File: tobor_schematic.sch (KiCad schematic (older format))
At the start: 25 parts, among them SW1 Bin detect right, SW2 Bin detect left, U1 LM7805_TO220, U10 TCRT5000, U2 LM7833_TO220, U3 LM7805_TO220, U4 TCRT5000, U5 TCRT5000

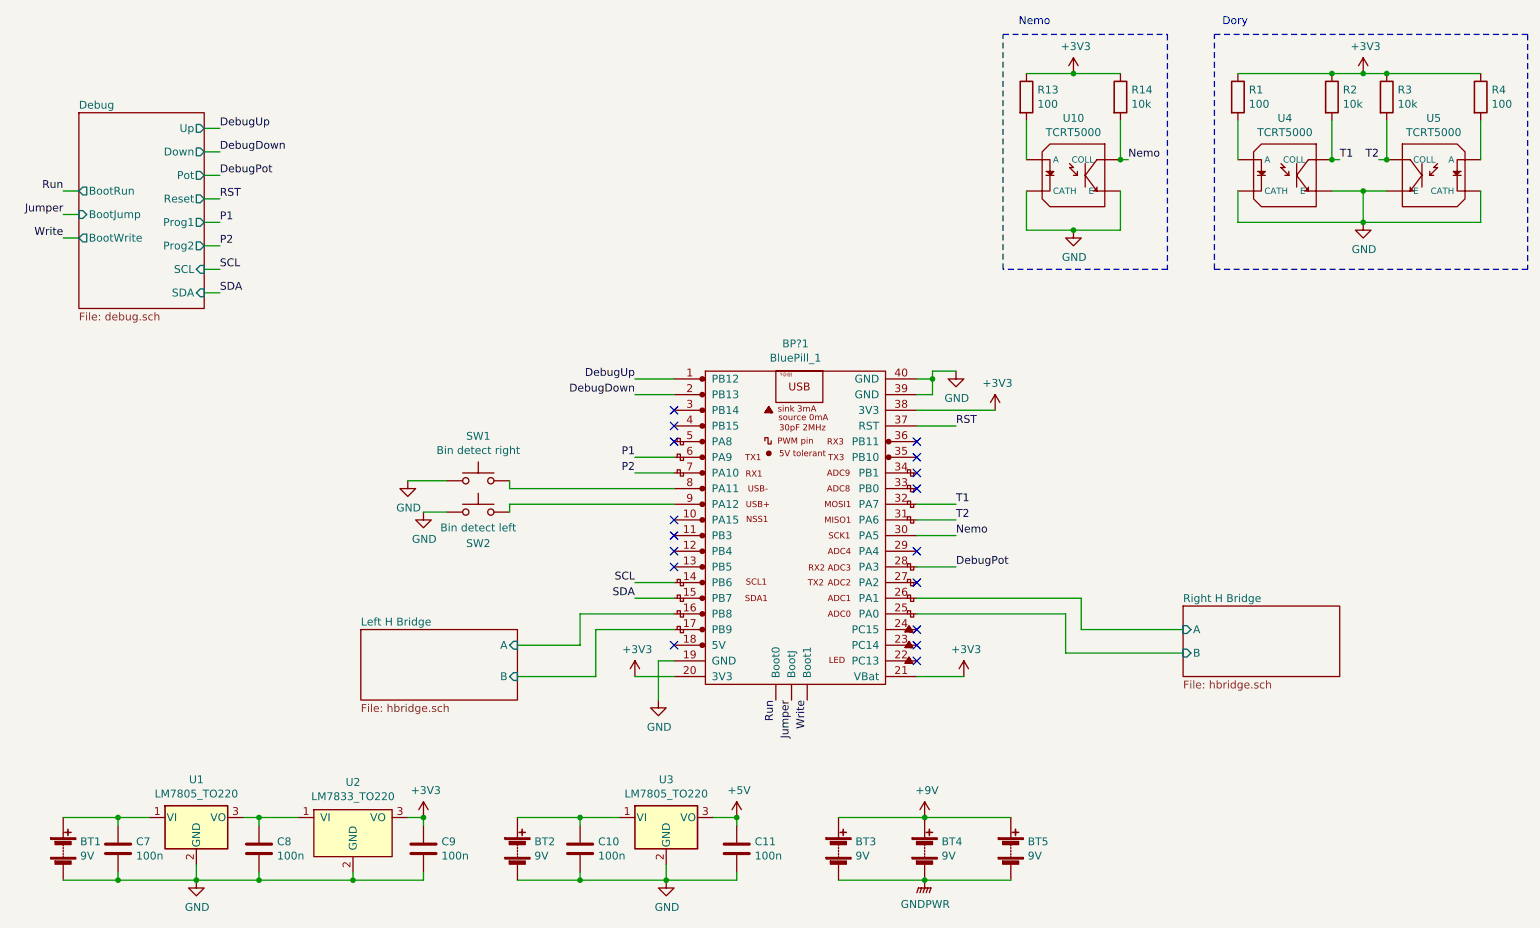
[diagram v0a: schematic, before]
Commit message: Add servos and can brush motor
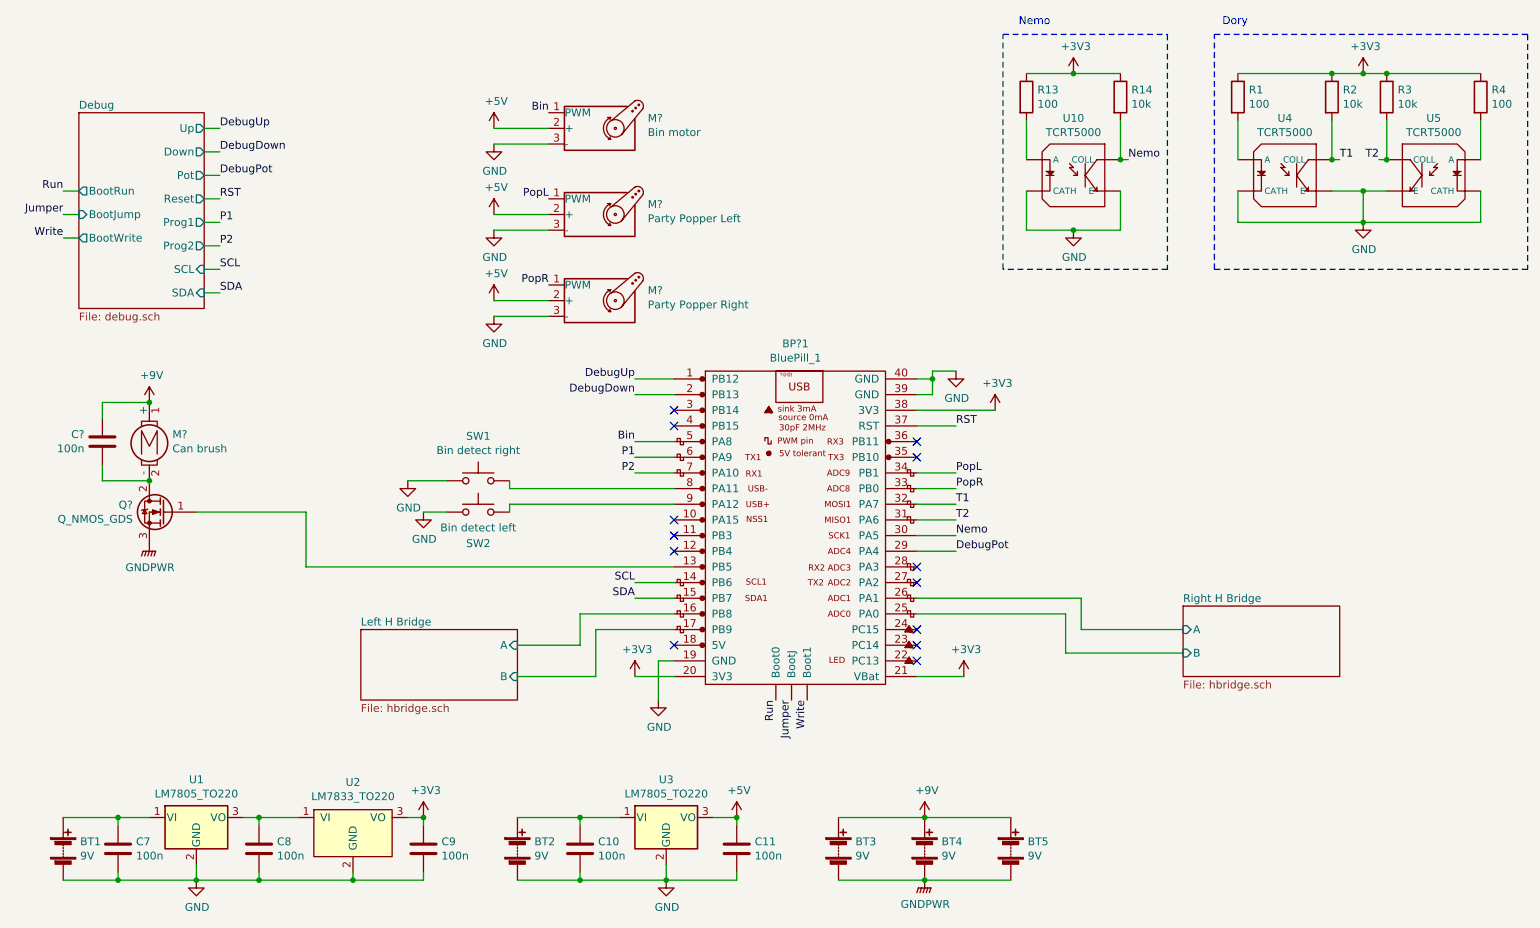
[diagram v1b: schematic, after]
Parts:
- added C?: 100n, symbol Device:C
- added M?: Bin motor, symbol Motor:Motor_Servo
- added M?: Party Popper Left, symbol Motor:Motor_Servo
- added M?: Party Popper Right, symbol Motor:Motor_Servo
- added M?: Can brush, symbol Motor:Motor_DC_ALT
- added Q?: Q_NMOS_GDS, symbol Device:Q_NMOS_GDS
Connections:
- net +5V: now also M?.2 (+), M?.2 (+), M?.2 (+)
- net +9V: now also C?.2, M?.1 (+)
- net DebugPot: now also BP?1.29 (PA4); no longer BP?1.28 (PA3)
- net GND: now also M?.3 (-), M?.3 (-), M?.3 (-)
- net GNDPWR: now also Q?.3 (S)
- net at BP?1.13 (PB5): now also Q?.1 (G)
- net PopR: now reaches BP?1.33 (PB0)
- net PopR: now also M?.1 (PWM)
- net PopL: now reaches BP?1.34 (PB1)
- net PopL: now also M?.1 (PWM)
- net Bin: now reaches BP?1.5 (PA8)
- net Bin: now also M?.1 (PWM)
- new net: C?.1, M?.2 (-), Q?.2 (D)
- no-connect marks 17 -> 13
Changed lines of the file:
@@
 NoConn ~ 5200 3250
 NoConn ~ 5200 3350
-NoConn ~ 5200 4250
 NoConn ~ 5200 4750
 NoConn ~ 6750 4850
@@
 Wire Wire Line
 	7000 4050 6750 4050
-Text Label 7000 4250 0    50   ~ 0
+Text Label 7000 4150 0    50   ~ 0
 DebugPot
-Wire Wire Line
-	7000 4250 6750 4250
 $Comp
 L STM32:BluePill_1 BP?1
@@
 NoConn ~ 5200 3950
 NoConn ~ 5200 4050
-NoConn ~ 5200 3450
-NoConn ~ 6750 3650
-NoConn ~ 6750 3750
-NoConn ~ 6750 4150
 Wire Wire Line
 	2200 1450 2300 1450
@@
 Wire Wire Line
 	6750 3250 7250 3250
+Wire Wire Line
+	7000 4150 6750 4150
+NoConn ~ 6750 4250
+$Comp
+L Motor:Motor_Servo M?
+U 1 1 5F00F8D5
+P 4700 1450
+F 0 "M?" H 5032 1515 50  0000 L CNN
+F 1 "Bin motor" H 5032 1424 50  0000 L CNN
+F 2 "" H 4700 1260 50  0001 C CNN
+F 3 "http://forums.parallax.com/uploads/attachments/46831/74481.png" H 4700 1260 50  0001 C CNN
+	1    4700 1450
+	1    0    0    -1
+$EndComp
+$Comp
+L Motor:Motor_Servo M?
+U 1 1 5F0107C0
+P 4700 2000
+F 0 "M?" H 5032 2065 50  0000 L CNN
+F 1 "Party Popper Left" H 5032 1974 50  0000 L CNN
+F 2 "" H 4700 1810 50  0001 C CNN
+F 3 "http://forums.parallax.com/uploads/attachments/46831/74481.png" H 4700 1810 50  0001 C CNN
+	1    4700 2000
+	1    0    0    -1
+$EndComp
+$Comp
+L Motor:Motor_Servo M?
+U 1 1 5F011350
+P 4700 2550
+F 0 "M?" H 5032 2615 50  0000 L CNN
+F 1 "Party Popper Right" H 5032 2524 50  0000 L CNN
+F 2 "" H 4700 2360 50  0001 C CNN
+F 3 "http://forums.parallax.com/uploads/attachments/46831/74481.png" H 4700 2360 50  0001 C CNN
+	1    4700 2550
+	1    0    0    -1
+$EndComp
+$Comp
+L power:+5V #PWR?
+U 1 1 5F0126EA
+P 4050 1450
+F 0 "#PWR?" H 4050 1300 50  0001 C CNN
+F 1 "+5V" H 4065 1623 50  0000 C CNN
+F 2 "" H 4050 1450 50  0001 C CNN
+F 3 "" H 4050 1450 50  0001 C CNN
+	1    4050 1450
+	1    0    0    -1
+$EndComp
+$Comp
+L power:+5V #PWR?
+U 1 1 5F012A59
+P 4050 2550
+F 0 "#PWR?" H 4050 2400 50  0001 C CNN
+F 1 "+5V" H 4065 2723 50  0000 C CNN
+F 2 "" H 4050 2550 50  0001 C CNN
+F 3 "" H 4050 2550 50  0001 C CNN
+	1    4050 2550
+	1    0    0    -1
+$EndComp
+$Comp
+L power:GND #PWR?
+U 1 1 5F01C8B6
+P 4050 1550
+F 0 "#PWR?" H 4050 1300 50  0001 C CNN
+F 1 "GND" H 4055 1377 50  0000 C CNN
+F 2 "" H 4050 1550 50  0001 C CNN
+F 3 "" H 4050 1550 50  0001 C CNN
+	1    4050 1550
+	1    0    0    -1
+$EndComp
+$Comp
+L power:GND #PWR?
+U 1 1 5F01CD54
+P 4050 2100
+F 0 "#PWR?" H 4050 1850 50  0001 C CNN
+F 1 "GND" H 4055 1927 50  0000 C CNN
+F 2 "" H 4050 2100 50  0001 C CNN
+F 3 "" H 4050 2100 50  0001 C CNN
+	1    4050 2100
+	1    0    0    -1
+$EndComp
+$Comp
+L power:+5V #PWR?
+U 1 1 5F0128A7
+P 4050 2000
+F 0 "#PWR?" H 4050 1850 50  0001 C CNN
+F 1 "+5V" H 4065 2173 50  0000 C CNN
+F 2 "" H 4050 2000 50  0001 C CNN
+F 3 "" H 4050 2000 50  0001 C CNN
+	1    4050 2000
+	1    0    0    -1
+$EndComp
+$Comp
+L power:GND #PWR?
+U 1 1 5F02E2B0
+P 4050 2650
+F 0 "#PWR?" H 4050 2400 50  0001 C CNN
+F 1 "GND" H 4055 2477 50  0000 C CNN
+F 2 "" H 4050 2650 50  0001 C CNN
+F 3 "" H 4050 2650 50  0001 C CNN
+	1    4050 2650
+	1    0    0    -1
+$EndComp
+Wire Wire Line
+	4050 2550 4400 2550
+Wire Wire Line
+	4400 2650 4050 2650
+Wire Wire Line
+	4050 2100 4400 2100
+Wire Wire Line
+	4400 2000 4050 2000
+Wire Wire Line
+	4050 1550 4400 1550
+Wire Wire Line
+	4400 1450 4050 1450
+Text Label 4400 1350 2    50   ~ 0
+Bin
+Text Label 4400 1900 2    50   ~ 0
+PopL
+Text Label 4400 2450 2    50   ~ 0
+PopR
+Text Label 4950 3450 2    50   ~ 0
+Bin
+Wire Wire Line
+	4950 3450 5200 3450
+Text Label 7000 3650 0    50   ~ 0
+PopL
+Text Label 7000 3750 0    50   ~ 0
+PopR
+Wire Wire Line
+	7000 3750 6750 3750
+Wire Wire Line
+	6750 3650 7000 3650
+$Comp
+L power:GNDPWR #PWR?
+U 1 1 5F0D4619
+P 1850 4100
+F 0 "#PWR?" H 1850 3900 50  0001 C CNN
+F 1 "GNDPWR" H 1854 3946 50  0000 C CNN
+F 2 "" H 1850 4050 50  0001 C CNN
+F 3 "" H 1850 4050 50  0001 C CNN
+	1    1850 4100
+	1    0    0    -1
+$EndComp
+$Comp
+L Device:Q_NMOS_GDS Q?
+U 1 1 5F0D2B87
+P 1950 3900
+F 0 "Q?" H 2156 3946 50  0000 L CNN
+F 1 "Q_NMOS_GDS" H 2156 3855 50  0000 L CNN
+F 2 "" H 2150 4000 50  0001 C CNN
+F 3 "~" H 1950 3900 50  0001 C CNN
+	1    1950 3900
+	-1   0    0    -1
+$EndComp
+Wire Wire Line
+	2150 3900 2850 3900
+Wire Wire Line
+	2850 3900 2850 4250
+Wire Wire Line
+	2850 4250 5200 4250
+$Comp
+L Motor:Motor_DC_ALT M?
+U 1 1 5F0ED853
+P 1850 3400
+F 0 "M?" H 1997 3396 50  0000 L CNN
+F 1 "Can brush" H 1997 3305 50  0000 L CNN
+F 2 "" H 1850 3310 50  0001 C CNN
+F 3 "~" H 1850 3310 50  0001 C CNN
+	1    1850 3400
+	1    0    0    -1
+$EndComp
+$Comp
+L Device:C C?
+U 1 1 5F0EEAE3
+P 1550 3450
+F 0 "C?" H 1435 3404 50  0000 R CNN
+F 1 "100n" H 1435 3495 50  0000 R CNN
+F 2 "" H 1588 3300 50  0001 C CNN
+F 3 "~" H 1550 3450 50  0001 C CNN
+	1    1550 3450
+	1    0    0    1
+$EndComp
+Wire Wire Line
+	1550 3600 1550 3700
+Wire Wire Line
+	1550 3700 1850 3700
+Connection ~ 1850 3700
+Wire Wire Line
+	1550 3300 1550 3200
+Wire Wire Line
+	1550 3200 1850 3200
+$Comp
+L power:+9V #PWR?
+U 1 1 5F0FAB23
+P 1850 3200
+F 0 "#PWR?" H 1850 3050 50  0001 C CNN
+F 1 "+9V" H 1865 3373 50  0000 C CNN
+F 2 "" H 1850 3200 50  0001 C CNN
+F 3 "" H 1850 3200 50  0001 C CNN
+	1    1850 3200
+	1    0    0    -1
+$EndComp
+Connection ~ 1850 3200
 $EndSCHEMATC

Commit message: Misc minor fixes
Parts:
- gave numbers to parts that had none: 6
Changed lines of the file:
@@
 NoConn ~ 6750 4250
 $Comp
-L Motor:Motor_Servo M?
+L Motor:Motor_Servo M4
 U 1 1 5F00F8D5
 P 4700 1450
-F 0 "M?" H 5032 1515 50  0000 L CNN
+F 0 "M4" H 5032 1515 50  0000 L CNN
 F 1 "Bin motor" H 5032 1424 50  0000 L CNN
 F 2 "" H 4700 1260 50  0001 C CNN
@@
 $EndComp
 $Comp
-L Motor:Motor_Servo M?
+L Motor:Motor_Servo M5
 U 1 1 5F0107C0
 P 4700 2000
-F 0 "M?" H 5032 2065 50  0000 L CNN
+F 0 "M5" H 5032 2065 50  0000 L CNN
 F 1 "Party Popper Left" H 5032 1974 50  0000 L CNN
 F 2 "" H 4700 1810 50  0001 C CNN
@@
 $EndComp
 $Comp
-L Motor:Motor_Servo M?
+L Motor:Motor_Servo M6
 U 1 1 5F011350
 P 4700 2550
-F 0 "M?" H 5032 2615 50  0000 L CNN
+F 0 "M6" H 5032 2615 50  0000 L CNN
 F 1 "Party Popper Right" H 5032 2524 50  0000 L CNN
 F 2 "" H 4700 2360 50  0001 C CNN
@@
 $EndComp
 $Comp
-L Device:Q_NMOS_GDS Q?
+L Device:Q_NMOS_GDS Q13
 U 1 1 5F0D2B87
 P 1950 3900
-F 0 "Q?" H 2156 3946 50  0000 L CNN
+F 0 "Q13" H 2156 3946 50  0000 L CNN
 F 1 "Q_NMOS_GDS" H 2156 3855 50  0000 L CNN
 F 2 "" H 2150 4000 50  0001 C CNN
@@
 	2850 4250 5200 4250
 $Comp
-L Motor:Motor_DC_ALT M?
+L Motor:Motor_DC_ALT M3
 U 1 1 5F0ED853
 P 1850 3400
-F 0 "M?" H 1997 3396 50  0000 L CNN
+F 0 "M3" H 1997 3396 50  0000 L CNN
 F 1 "Can brush" H 1997 3305 50  0000 L CNN
 F 2 "" H 1850 3310 50  0001 C CNN
@@
 $EndComp
 $Comp
-L Device:C C?
+L Device:C C14
 U 1 1 5F0EEAE3
 P 1550 3450
-F 0 "C?" H 1435 3404 50  0000 R CNN
+F 0 "C14" H 1435 3404 50  0000 R CNN
 F 1 "100n" H 1435 3495 50  0000 R CNN
 F 2 "" H 1588 3300 50  0001 C CNN
